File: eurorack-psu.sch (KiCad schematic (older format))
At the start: 30 parts, among them J1 Conn_02x08_Odd_Even, U1 LM317, U2 LM337

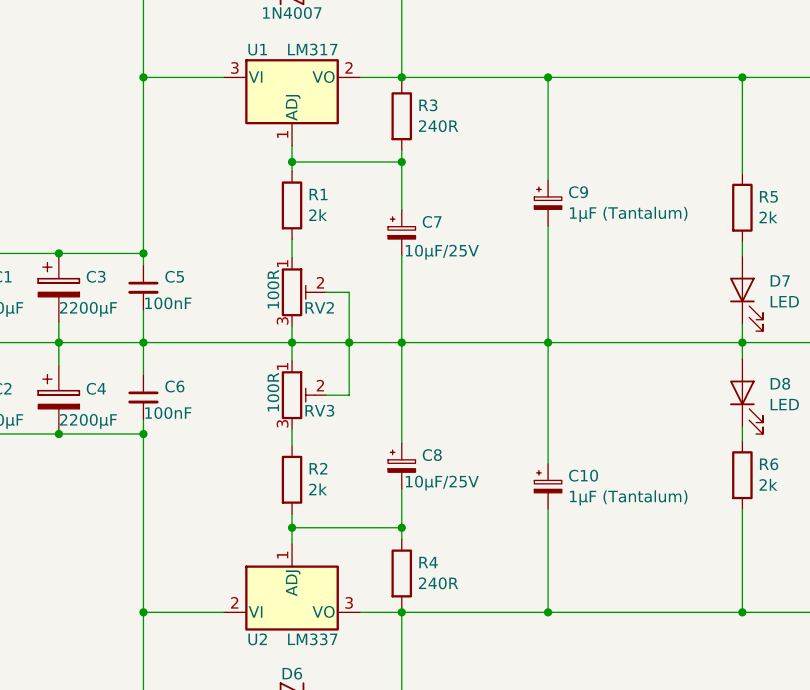
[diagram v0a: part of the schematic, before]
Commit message: rm oshw mark, tweak some stuff
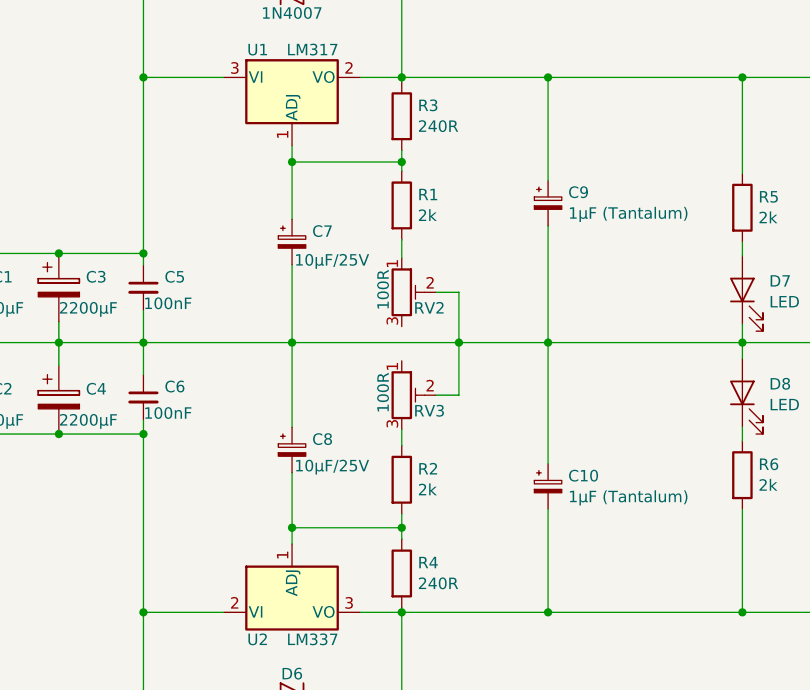
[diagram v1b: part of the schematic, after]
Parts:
- TR1: footprint footprints:Transformer_Toroidal_D74.0mm -> footprints:Transformer_Toroidal_D74.0mm_OffBoardMount
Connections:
- net GNDREF: no longer RV2.3, RV3.1
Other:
- moved on the sheet: C7, C8, R1, R2, RV2, RV3
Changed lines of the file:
@@
 L Device:R R2
 U 1 1 5BDE77C6
-P 5930 3430
-F 0 "R2" H 6000 3476 50  0000 L CNN
-F 1 "2k" H 6000 3385 50  0000 L CNN
-F 2 "Resistors_ThroughHole:R_Axial_DIN0207_L6.3mm_D2.5mm_P7.62mm_Horizontal" V 5860 3430 50  0001 C CNN
-F 3 "~" H 5930 3430 50  0001 C CNN
-	1    5930 3430
+P 6410 3430
+F 0 "R2" H 6480 3476 50  0000 L CNN
+F 1 "2k" H 6480 3385 50  0000 L CNN
+F 2 "Resistors_ThroughHole:R_Axial_DIN0207_L6.3mm_D2.5mm_P7.62mm_Horizontal" V 6340 3430 50  0001 C CNN
+F 3 "~" H 6410 3430 50  0001 C CNN
+	1    6410 3430
 	1    0    0    -1
 $EndComp
@@
 L Device:R R1
 U 1 1 5BDE7832
-P 5930 2230
-F 0 "R1" H 6000 2276 50  0000 L CNN
-F 1 "2k" H 6000 2185 50  0000 L CNN
-F 2 "Resistors_ThroughHole:R_Axial_DIN0207_L6.3mm_D2.5mm_P7.62mm_Horizontal" V 5860 2230 50  0001 C CNN
-F 3 "~" H 5930 2230 50  0001 C CNN
-	1    5930 2230
+P 6410 2230
+F 0 "R1" H 6480 2276 50  0000 L CNN
+F 1 "2k" H 6480 2185 50  0000 L CNN
+F 2 "Resistors_ThroughHole:R_Axial_DIN0207_L6.3mm_D2.5mm_P7.62mm_Horizontal" V 6340 2230 50  0001 C CNN
+F 3 "~" H 6410 2230 50  0001 C CNN
+	1    6410 2230
 	1    0    0    -1
 $EndComp
@@
 L Device:CP_Small C7
 U 1 1 5BDE7AA3
-P 6410 2350
-F 0 "C7" H 6498 2396 50  0000 L CNN
-F 1 "10µF/25V" H 6420 2270 50  0000 L CNN
-F 2 "Capacitors_ThroughHole:CP_Radial_D5.0mm_P2.00mm" H 6410 2350 50  0001 C CNN
-F 3 "~" H 6410 2350 50  0001 C CNN
-	1    6410 2350
+P 5930 2390
+F 0 "C7" H 6018 2436 50  0000 L CNN
+F 1 "10µF/25V" H 5940 2310 50  0000 L CNN
+F 2 "Capacitors_ThroughHole:CP_Radial_D5.0mm_P2.00mm" H 5930 2390 50  0001 C CNN
+F 3 "~" H 5930 2390 50  0001 C CNN
+	1    5930 2390
 	1    0    0    -1
 $EndComp
@@
 $EndComp
 Connection ~ 5280 2830
-Wire Wire Line
-	5280 2830 5930 2830
-Connection ~ 5930 2830
 $Comp
 L Device:R_POT_TRIM RV2
 U 1 1 5BDFCB27
-P 5930 2610
-F 0 "RV2" H 6120 2540 50  0000 R CNN
-F 1 "100R" V 5850 2710 50  0000 R CNN
-F 2 "Potentiometers:Potentiometer_Trimmer_Bourns_3266P" H 5930 2610 50  0001 C CNN
-F 3 "~" H 5930 2610 50  0001 C CNN
-	1    5930 2610
+P 6410 2610
+F 0 "RV2" H 6600 2540 50  0000 R CNN
+F 1 "100R" V 6330 2710 50  0000 R CNN
+F 2 "Potentiometers:Potentiometer_Trimmer_Bourns_3266P" H 6410 2610 50  0001 C CNN
+F 3 "~" H 6410 2610 50  0001 C CNN
+	1    6410 2610
 	1    0    0    -1
 $EndComp
@@
 L Device:R_POT_TRIM RV3
 U 1 1 5BDFCF29
-P 5930 3060
-F 0 "RV3" H 6120 2990 50  0000 R CNN
-F 1 "100R" V 5850 3160 50  0000 R CNN
-F 2 "Potentiometers:Potentiometer_Trimmer_Bourns_3266P" H 5930 3060 50  0001 C CNN
-F 3 "~" H 5930 3060 50  0001 C CNN
-	1    5930 3060
+P 6410 3060
+F 0 "RV3" H 6600 2990 50  0000 R CNN
+F 1 "100R" V 6330 3160 50  0000 R CNN
+F 2 "Potentiometers:Potentiometer_Trimmer_Bourns_3266P" H 6410 3060 50  0001 C CNN
+F 3 "~" H 6410 3060 50  0001 C CNN
+	1    6410 3060
 	1    0    0    -1
 $EndComp
@@
 Connection ~ 5930 2040
 Wire Wire Line
-	5930 2040 5930 2080
-Connection ~ 6410 2040
-Wire Wire Line
-	6410 2040 6410 2250
-Wire Wire Line
-	6410 2450 6410 2830
-Wire Wire Line
-	6410 2830 6180 2830
-Wire Wire Line
 	6230 1670 6410 1670
 Wire Wire Line
 	6410 1670 6410 1690
 Wire Wire Line
-	6080 2610 6180 2610
-Connection ~ 6180 2830
-Wire Wire Line
-	6180 2830 5930 2830
-Wire Wire Line
-	6080 3060 6180 3060
+	6560 2610 6660 2610
+Wire Wire Line
+	6560 3060 6660 3060
 $Comp
 L Device:R R4
@@
 L Device:CP_Small C8
 U 1 1 5BE339A8
-P 6410 3370
-F 0 "C8" H 6498 3416 50  0000 L CNN
-F 1 "10µF/25V" H 6420 3300 50  0000 L CNN
-F 2 "Capacitors_ThroughHole:CP_Radial_D5.0mm_P2.00mm" H 6410 3370 50  0001 C CNN
-F 3 "~" H 6410 3370 50  0001 C CNN
-	1    6410 3370
+P 5930 3300
+F 0 "C8" H 6018 3346 50  0000 L CNN
+F 1 "10µF/25V" H 5940 3230 50  0000 L CNN
+F 2 "Capacitors_ThroughHole:CP_Radial_D5.0mm_P2.00mm" H 5930 3300 50  0001 C CNN
+F 3 "~" H 5930 3300 50  0001 C CNN
+	1    5930 3300
 	1    0    0    -1
 $EndComp
@@
 Wire Wire Line
 	5930 3640 6410 3640
-Connection ~ 6410 3640
-Wire Wire Line
-	6410 3640 6410 3470
 Wire Wire Line
 	6230 4010 6410 4010
 Wire Wire Line
 	6410 4010 6410 3990
-Connection ~ 5930 3640
-Wire Wire Line
-	5930 3640 5930 3580
-Wire Wire Line
-	6410 2830 6410 3270
-Connection ~ 6410 2830
-Wire Wire Line
-	6180 2610 6180 2830
-Wire Wire Line
-	5930 2760 5930 2830
-Wire Wire Line
-	5930 3210 5930 3280
-Wire Wire Line
-	5930 2830 5930 2910
-Wire Wire Line
-	6180 2830 6180 3060
-Wire Wire Line
-	5930 2460 5930 2380
+Wire Wire Line
+	6410 3640 6410 3580
+Wire Wire Line
+	6660 2610 6660 2830
+Wire Wire Line
+	6410 3210 6410 3280
+Wire Wire Line
+	6660 2830 6660 3060
+Wire Wire Line
+	6410 2460 6410 2380
 Wire Wire Line
 	7050 2320 7050 2830
 Wire Wire Line
-	7050 2830 6410 2830
+	7050 2830 6660 2830
 $Comp
 L Device:CP_Small C10
@@
 F 0 "TR1" H 2120 3362 50  0000 C CNN
 F 1 "VPT30-830" H 2120 3271 50  0000 C CNN
-F 2 "footprints:Transformer_Toroidal_D74.0mm" H 2120 2880 50  0001 C CNN
+F 2 "footprints:Transformer_Toroidal_D74.0mm_OffBoardMount" H 2120 2880 50  0001 C CNN
 F 3 "" H 2120 2880 50  0001 C CNN
 	1    2120 2880
@@
 Wire Wire Line
 	8540 4010 8650 4010
+Wire Wire Line
+	5280 2830 5930 2830
+Wire Wire Line
+	5930 3200 5930 2830
+Connection ~ 5930 2830
+Wire Wire Line
+	5930 3400 5930 3640
+Connection ~ 5930 3640
+Connection ~ 6410 3640
+Connection ~ 6660 2830
+Wire Wire Line
+	5930 2830 6660 2830
+Wire Wire Line
+	5930 2040 5930 2290
+Wire Wire Line
+	5930 2490 5930 2830
+Wire Wire Line
+	6410 2040 6410 2080
+Connection ~ 6410 2040
 $EndSCHEMATC
